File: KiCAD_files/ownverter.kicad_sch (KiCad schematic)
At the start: 10 parts, among them J101 Harting-15 and Wago 6

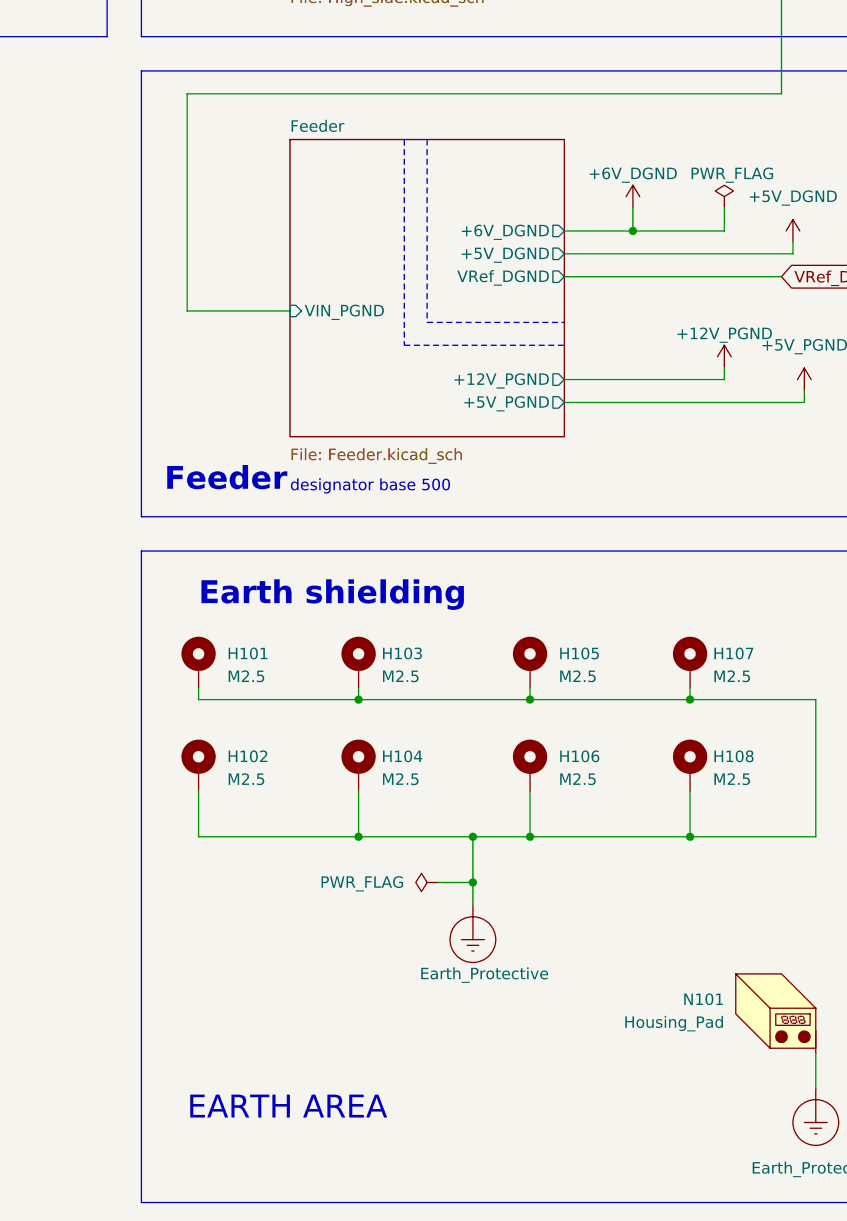
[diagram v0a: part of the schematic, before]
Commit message: Added netclasses and ERC rules for isolation clearances
Signed-off-by: Jean Alinei <jean.alinei@laas.fr>
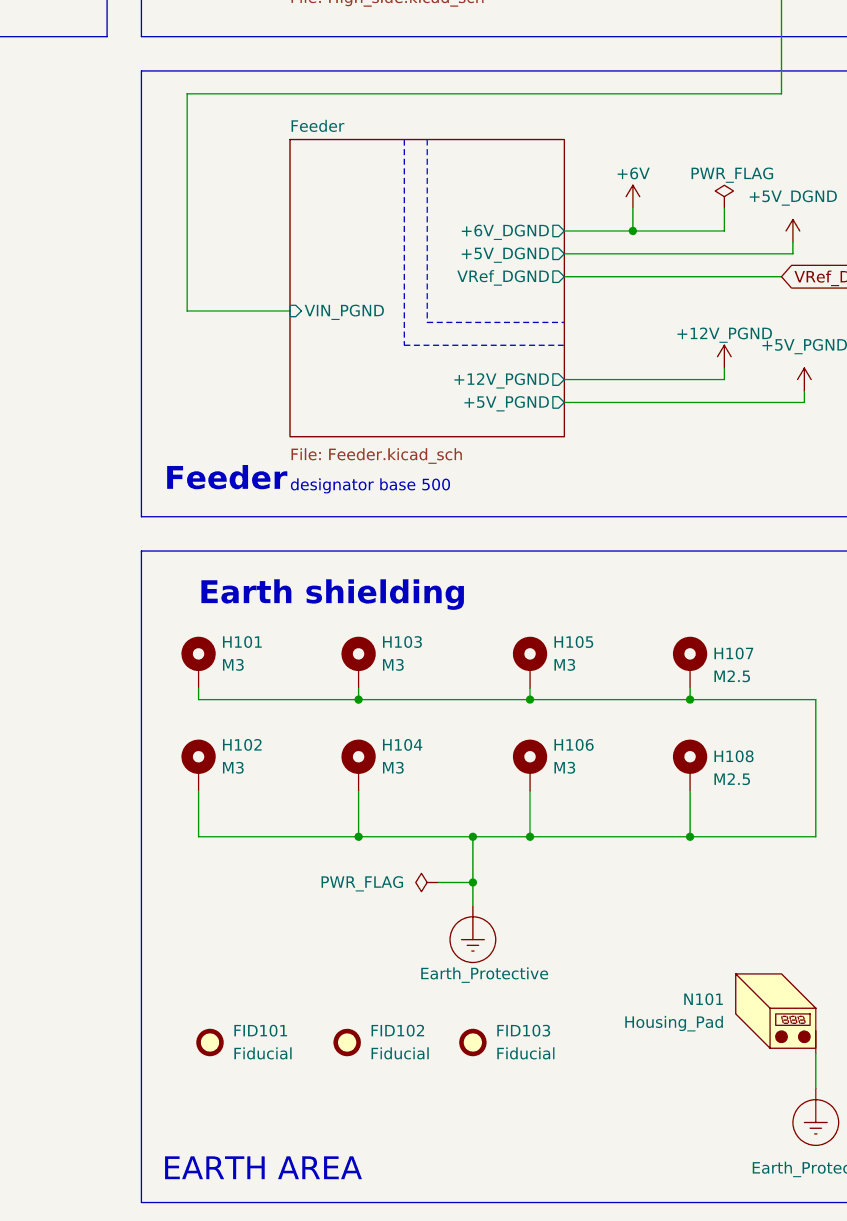
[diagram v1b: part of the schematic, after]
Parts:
- added FID101, FID102, FID103: Fiducial, Fiducial:Fiducial_0.75mm_Mask1.5mm, symbol Mechanical:Fiducial
- H101, H102, H103, H104, H105, H106: value M2.5 -> M3; footprint MountingHole:MountingHole_2.7mm_M2.5_DIN965_Pad_TopOnly -> MountingHole:MountingHole_3.2mm_M3_DIN965_Pad_TopOnly
